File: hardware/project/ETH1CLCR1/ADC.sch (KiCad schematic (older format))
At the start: 103 parts, among them Q1101 BC847W, Q1102 BC847W, Q1103 BC847W, Q1104 BC847W, U1101 ADG419BR, U1102 ADG419BR, U1103 ADR4525BRZ, U1104 ADA4807-2ARM, U1106 AD7380, U1106 ADA4807-2ARM, U1107 ADA4807-1AKSZ-R2, U1108 LT6350, U1109 LT6350, U1110 OPA602, U1111 OPA602, U1112 PGA103, U1113 PGA103

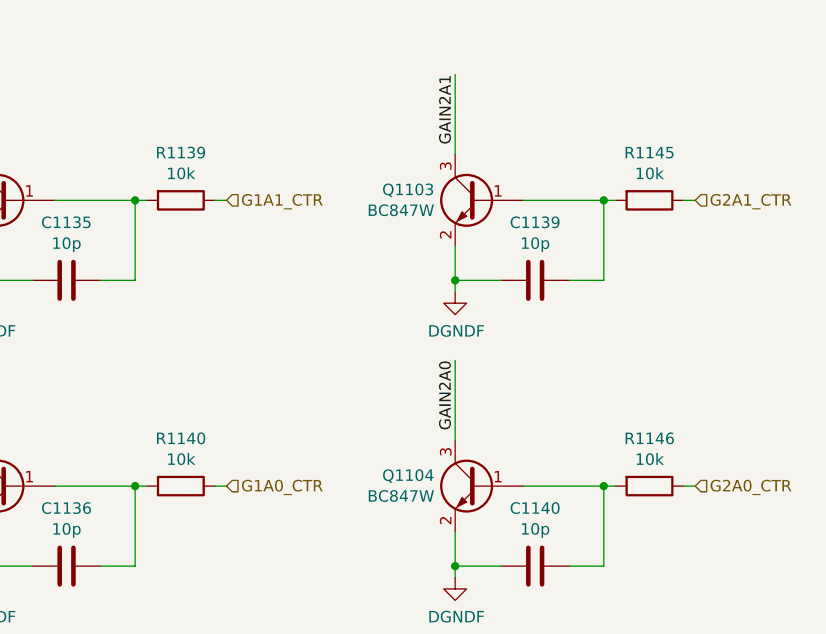
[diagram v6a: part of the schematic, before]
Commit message: Range BC847 base serial resistors value from 10k to 1k.
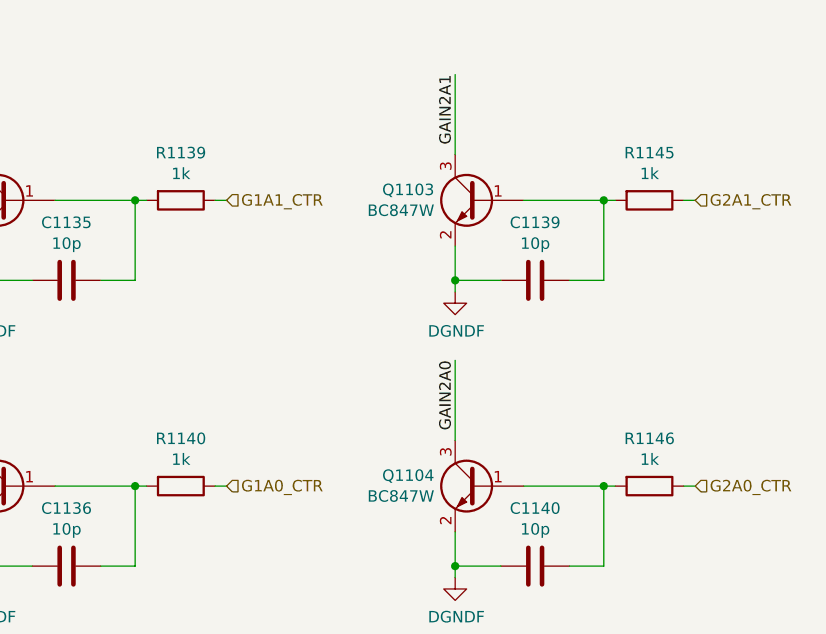
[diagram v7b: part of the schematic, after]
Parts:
- R1139, R1140, R1145, R1146: value 10k -> 1k
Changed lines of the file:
@@
 AR Path="/5E402F62/5E39CEEC" Ref="R1140"  Part="1"
 F 0 "R1140" V 12893 9150 50  0000 C CNN
-F 1 "10k" V 12984 9150 50  0000 C CNN
+F 1 "1k" V 12984 9150 50  0000 C CNN
 F 2 "Resistor_SMD:R_0603_1608Metric_Pad1.05x0.95mm_HandSolder" V 13030 9150 50  0001 C CNN
 F 3 "~" H 13100 9150 50  0001 C CNN
@@
 AR Path="/5E402F62/5E39CF11" Ref="R1139"  Part="1"
 F 0 "R1139" V 12893 7900 50  0000 C CNN
-F 1 "10k" V 12984 7900 50  0000 C CNN
+F 1 "1k" V 12984 7900 50  0000 C CNN
 F 2 "Resistor_SMD:R_0603_1608Metric_Pad1.05x0.95mm_HandSolder" V 13030 7900 50  0001 C CNN
 F 3 "~" H 13100 7900 50  0001 C CNN
@@
 AR Path="/5E402F62/5E39CF36" Ref="R1146"  Part="1"
 F 0 "R1146" V 14943 9150 50  0000 C CNN
-F 1 "10k" V 15034 9150 50  0000 C CNN
+F 1 "1k" V 15034 9150 50  0000 C CNN
 F 2 "Resistor_SMD:R_0603_1608Metric_Pad1.05x0.95mm_HandSolder" V 15080 9150 50  0001 C CNN
 F 3 "~" H 15150 9150 50  0001 C CNN
@@
 AR Path="/5E402F62/5E39CF5B" Ref="R1145"  Part="1"
 F 0 "R1145" V 14943 7900 50  0000 C CNN
-F 1 "10k" V 15034 7900 50  0000 C CNN
+F 1 "1k" V 15034 7900 50  0000 C CNN
 F 2 "Resistor_SMD:R_0603_1608Metric_Pad1.05x0.95mm_HandSolder" V 15080 7900 50  0001 C CNN
 F 3 "~" H 15150 7900 50  0001 C CNN

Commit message: BOM list update
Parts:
- R1144: value 10K -> 10k
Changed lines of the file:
@@
 P 14350 5000
 F 0 "R1144" V 14143 5000 50  0000 C CNN
-F 1 "10K" V 14234 5000 50  0000 C CNN
+F 1 "10k" V 14234 5000 50  0000 C CNN
 F 2 "Resistor_SMD:R_0603_1608Metric_Pad1.05x0.95mm_HandSolder" V 14280 5000 50  0001 C CNN
 F 3 "~" H 14350 5000 50  0001 C CNN
